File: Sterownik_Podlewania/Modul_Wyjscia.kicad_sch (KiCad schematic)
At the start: 7 parts

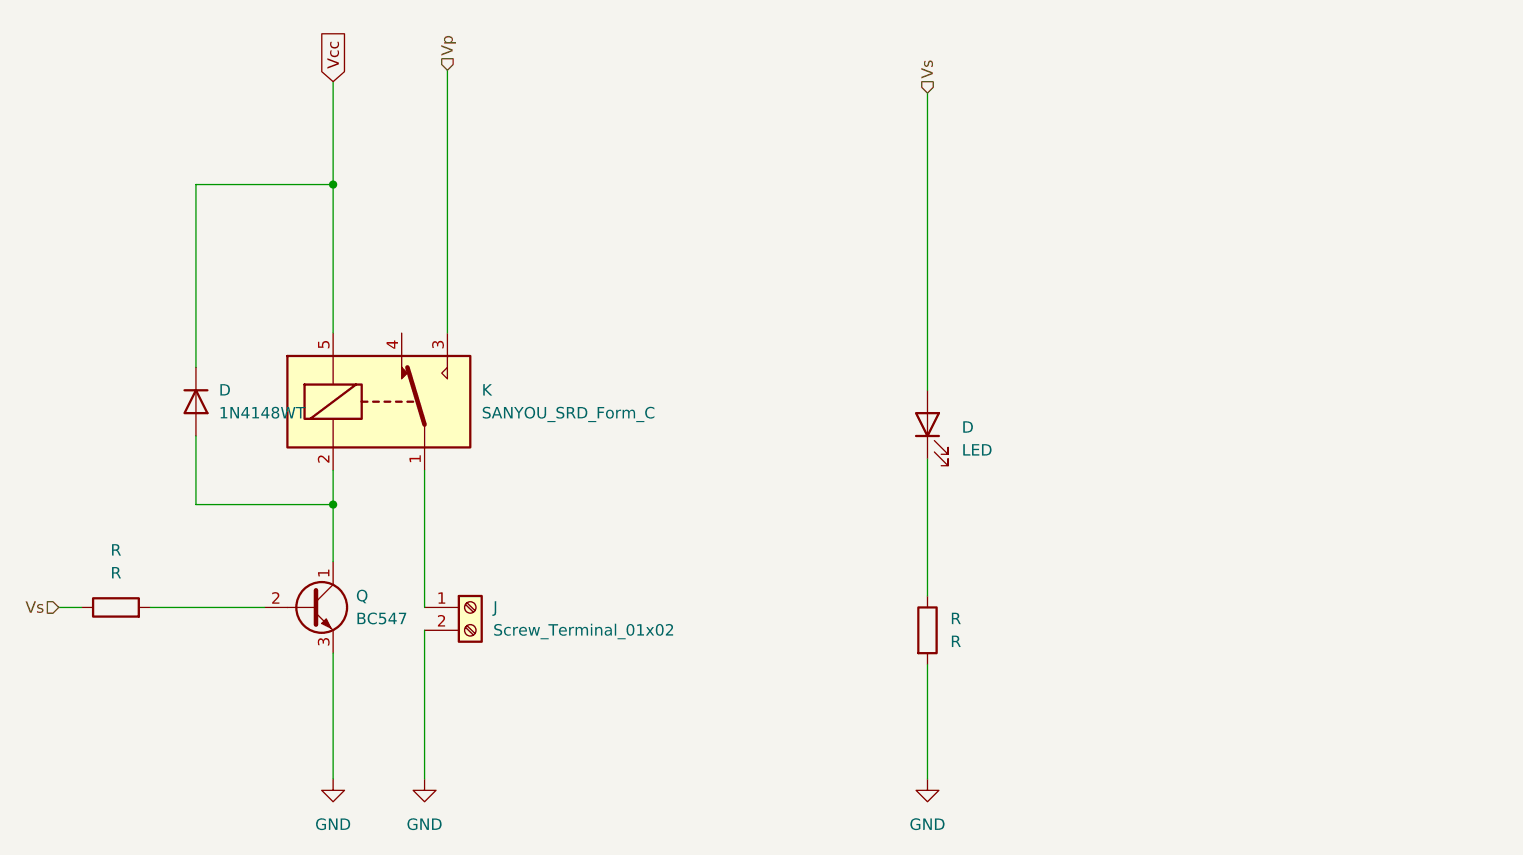
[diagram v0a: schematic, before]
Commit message: Dodanie zasilania, sekcji czujników światła, modyfikacja przełączników, dodanie znaczników
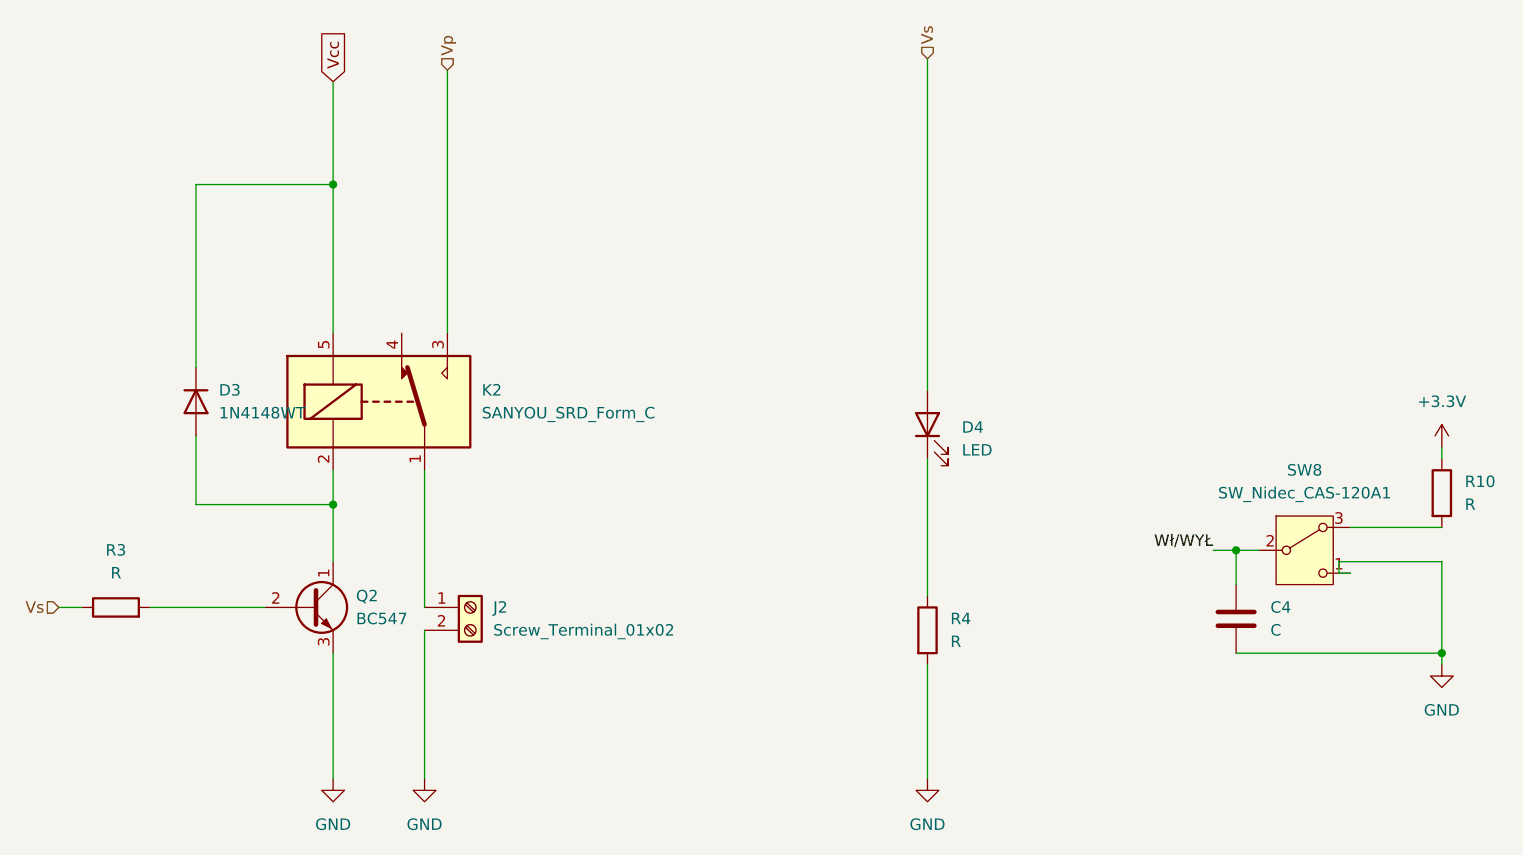
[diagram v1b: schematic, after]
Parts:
- added C4: C, symbol Device:C
- added R10: R, symbol Device:R
- added SW8: SW_Nidec_CAS-120A1, Button_Switch_SMD:Nidec_Copal_CAS-120A, symbol Switch:SW_Nidec_CAS-120A1
- renumbered D to D3, D to D4, J to J2, K to K2, Q to Q2, R to R3, R to R4
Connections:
- net GND: now also C4.2, SW8.1 (C)
- new net: R10.2, SW8.3 (A)
- new net +3.3V: R10.1
- new net Wł/WYŁ: C4.1, SW8.2 (B)

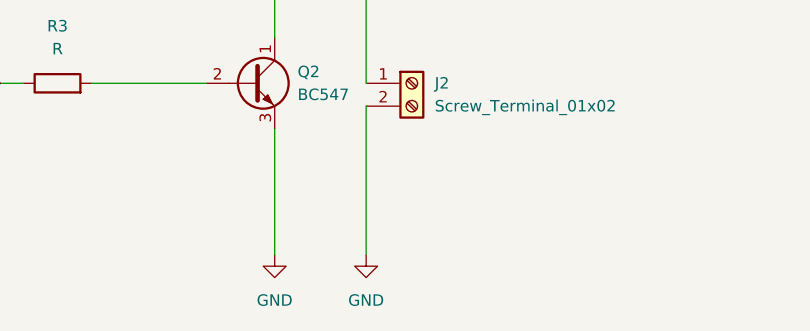
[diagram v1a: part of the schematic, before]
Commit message: Modyfikacja sekcji czujników
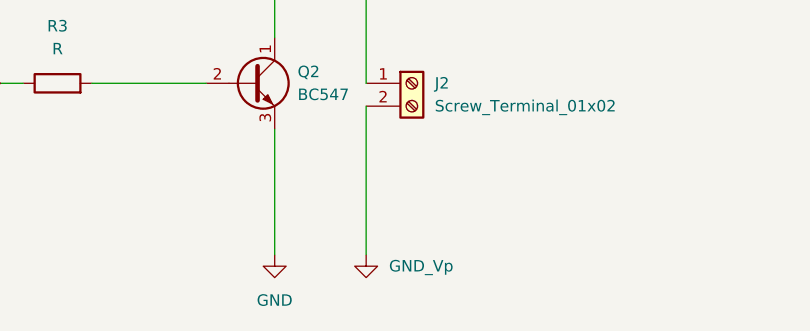
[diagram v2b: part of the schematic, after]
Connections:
- net GND: no longer J2.2 (Pin_2)
- new net GND_Vp: J2.2 (Pin_2)
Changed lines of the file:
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@@
 			)
 		)
-		(property "Value" "GND"
-			(at 147.32 120.65 0)
+		(property "Value" "GND_Vp"
+			(at 149.86 116.8399 0)
 			(effects
 				(font
 					(size 1.27 1.27)
 				)
+				(justify left)
 			)
 		)
